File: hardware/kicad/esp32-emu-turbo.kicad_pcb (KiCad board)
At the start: 4 copper layers, 160 x 75 mm, 81 parts, among them J1 USB-C-16P, J3 JST-PH-2P, J4 FPC-40P-0.5mm, SW1 SW-SMD-5.1x5.1, SW10 SW-SMD-5.1x5.1, SW11 SW-SMD-5.1x5.1, SW12 SW-SMD-5.1x5.1, SW13 SW-SMD-5.1x5.1, SW2 SW-SMD-5.1x5.1, SW3 SW-SMD-5.1x5.1, SW4 SW-SMD-5.1x5.1, SW5 SW-SMD-5.1x5.1, SW6 SW-SMD-5.1x5.1, SW7 SW-SMD-5.1x5.1, SW8 SW-SMD-5.1x5.1, SW9 SW-SMD-5.1x5.1, U1 ESP32-S3-WROOM-1-N16R8, U2 ESOP-8, U3 SOT-223, U5 SOP-16, U6 TF-01A

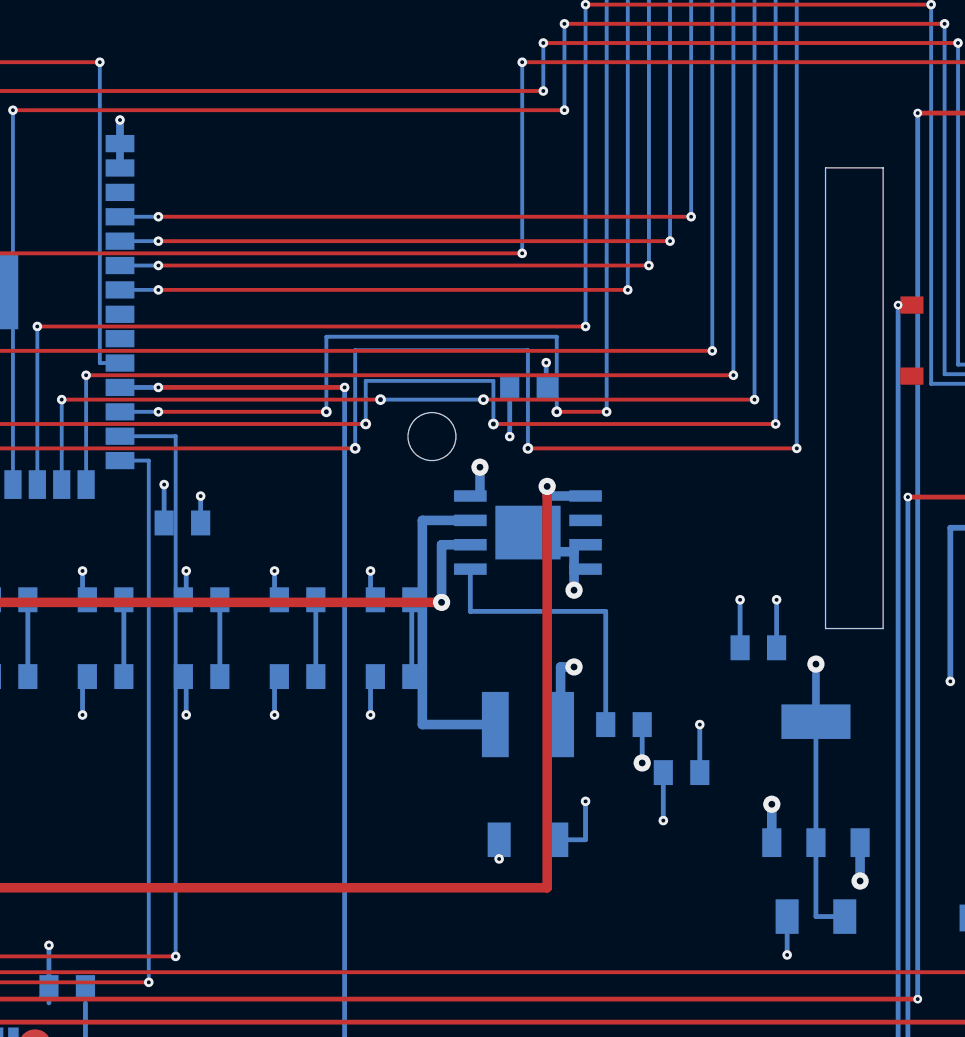
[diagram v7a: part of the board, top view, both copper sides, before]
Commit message: fix(pcb): thermal vias AMS1117 + LED nets + power trace widening
P1: Add 4 thermal vias (0.50/0.20mm) under AMS1117 tab pad for
    heat dissipation to In2.Cu +3V3 zone (0.85W at load)
P3: Add LED1_RA/LED2_RA nets for R17→LED1 and R18→LED2 connections
    (charging indicator LEDs were unrouted)
P4: Widen +3V3 main delivery traces from 0.4mm to 0.5mm (W_PWR)

Known remaining: BTN_X/Y F.Cu channels cross J1 shield pads
(structural issue requiring architectural reroute)

Results: 114/114 DFM + 9/9 DFA

Co-Authored-By: Claude Opus 4.6 (1M context) <noreply@anthropic.com>
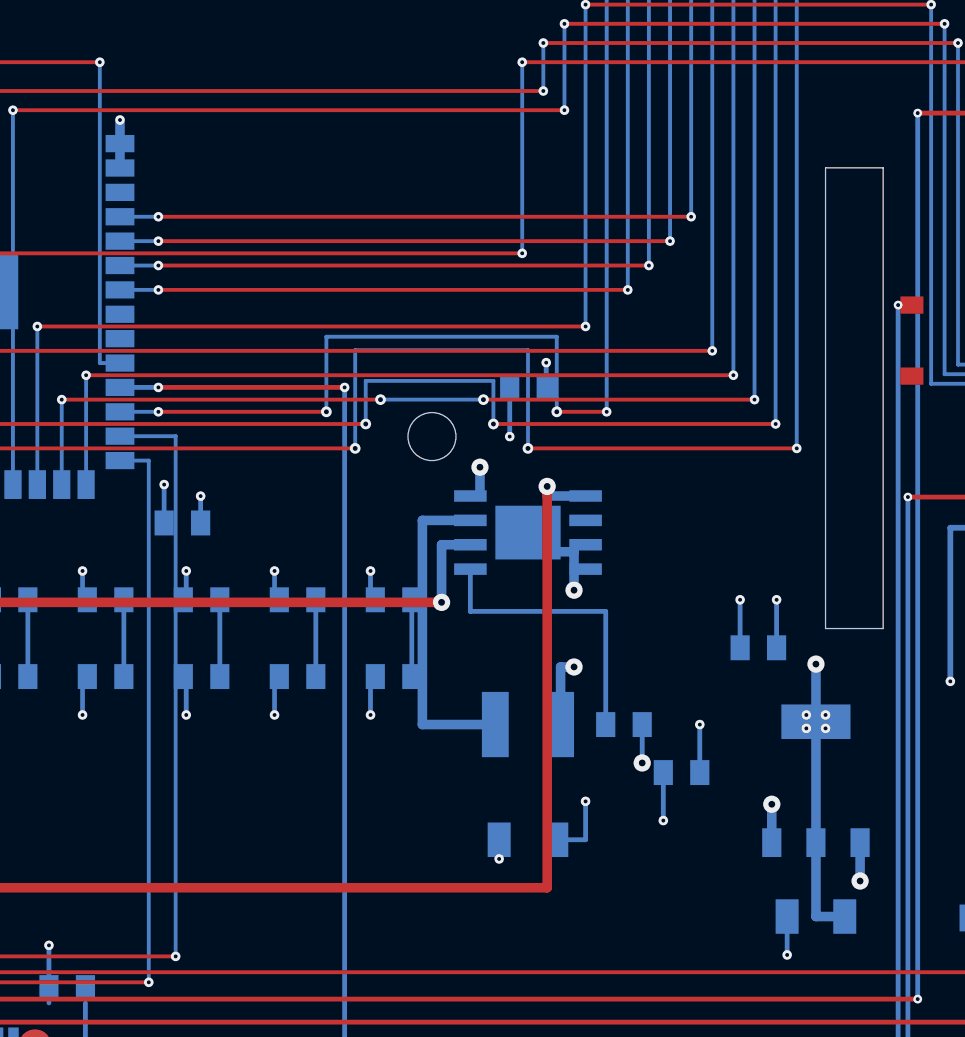
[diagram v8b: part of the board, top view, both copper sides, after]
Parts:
- removed the C25 at (31.5, 37.5)
- removed the SW10 at (28.0, 54.5)
- added FID1: Fiducial, Fiducial, F.Cu at (5.00, 5.00)
- added LED1: LED_0805, LED_0805, F.Cu at (25.0, 67.5)
- C25: renamed from FID1; value Fiducial -> C_0805; footprint Fiducial -> C_0805; moved to B.Cu
- SW10: renamed from LED1; value LED_0805 -> SW-SMD-5.1x5.1; footprint LED_0805 -> SW-SMD-5.1x5.1
- moved C25 41.9 mm to (31.5, 37.5)
- moved SW10 13.3 mm to (28.0, 54.5)
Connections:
- C25 pad 1: (no net) -> +5V
- LED2 pad 2: (no net) -> LED2_RA
- R17 pad 1: (no net) -> LED1_RA
- R18 pad 1: (no net) -> LED2_RA
- SW10 pad 1: GND -> (no net)
- SW10 pad 2: (no net) -> BTN_SELECT
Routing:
- net (no net): track 5.00 -> 0.00 mm, vias 2 -> 0
- net LED2_RA: track 0.00 -> 2.50 mm, vias 0 -> 1
- net LED1_RA: track 0.00 -> 2.50 mm, vias 0 -> 1
- net +3V3: track 59.1 -> 61.1 mm, vias 22 -> 26
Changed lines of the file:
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@@
   (net 49 "USB_CC2")
   (net 50 "PAM_VREF")
+  (net 51 "LED1_RA")
+  (net 52 "LED2_RA")
   (gr_line (start 6.0 0) (end 154.0 0) (stroke (width 0.05) (type default)) (layer "Edge.Cuts"))
   (gr_line (start 160.0 6.0) (end 160.0 69.0) (stroke (width 0.05) (type default)) (layer "Edge.Cuts"))
@@
     (property "Value" "LED_0805" (at 0 3 0) (layer "F.Fab") (effects (font (size 0.6 0.6) (thickness 0.2))))
     (pad "1" smd rect (at -0.95 0) (size 1.0 1.3) (layers "F.Cu" "F.Paste" "F.Mask") (net 1 "GND"))
-    (pad "2" smd rect (at 0.95 0) (size 1.0 1.3) (layers "F.Cu" "F.Paste" "F.Mask") (net 0 ""))
+    (pad "2" smd rect (at 0.95 0) (size 1.0 1.3) (layers "F.Cu" "F.Paste" "F.Mask") (net 51 "LED1_RA"))
   )
   (footprint "LED_0805" (at 32.0 67.5) (layer "F.Cu")
@@
     (property "Value" "LED_0805" (at 0 3 0) (layer "F.Fab") (effects (font (size 0.6 0.6) (thickness 0.2))))
     (pad "1" smd rect (at -0.95 0) (size 1.0 1.3) (layers "F.Cu" "F.Paste" "F.Mask") (net 1 "GND"))
-    (pad "2" smd rect (at 0.95 0) (size 1.0 1.3) (layers "F.Cu" "F.Paste" "F.Mask") (net 0 ""))
+    (pad "2" smd rect (at 0.95 0) (size 1.0 1.3) (layers "F.Cu" "F.Paste" "F.Mask") (net 52 "LED2_RA"))
   )
   (footprint "ESP32-S3-WROOM-1-N16R8" (at 80.0 27.5) (layer "B.Cu")
@@
     (property "Reference" "R17" (at 0 -3 0) (layer "B.Fab") (effects (font (size 0.6 0.6) (thickness 0.2)) (justify mirror)))
     (property "Value" "R_0805" (at 0 3 0) (layer "B.Fab") (effects (font (size 0.6 0.6) (thickness 0.2)) (justify mirror)))
-    (pad "1" smd rect (at 0.95 0) (size 1.0 1.3) (layers "B.Cu" "B.Paste" "B.Mask") (net 0 ""))
+    (pad "1" smd rect (at 0.95 0) (size 1.0 1.3) (layers "B.Cu" "B.Paste" "B.Mask") (net 51 "LED1_RA"))
     (pad "2" smd rect (at -0.95 0) (size 1.0 1.3) (layers "B.Cu" "B.Paste" "B.Mask") (net 4 "+3V3"))
   )
@@
     (property "Reference" "R18" (at 0 -3 0) (layer "B.Fab") (effects (font (size 0.6 0.6) (thickness 0.2)) (justify mirror)))
     (property "Value" "R_0805" (at 0 3 0) (layer "B.Fab") (effects (font (size 0.6 0.6) (thickness 0.2)) (justify mirror)))
-    (pad "1" smd rect (at 0.95 0) (size 1.0 1.3) (layers "B.Cu" "B.Paste" "B.Mask") (net 0 ""))
+    (pad "1" smd rect (at 0.95 0) (size 1.0 1.3) (layers "B.Cu" "B.Paste" "B.Mask") (net 52 "LED2_RA"))
     (pad "2" smd rect (at -0.95 0) (size 1.0 1.3) (layers "B.Cu" "B.Paste" "B.Mask") (net 4 "+3V3"))
   )
@@
   (segment (start 115.95 52.5) (end 115.95 54.5) (width 0.25) (layer "B.Cu") (net 3))
   (via (at 115.95 54.5) (size 0.9) (drill 0.35) (layers "F.Cu" "B.Cu") (net 3))
-  (segment (start 125.0 52.35) (end 125.0 49.35) (width 0.4) (layer "B.Cu") (net 4))
+  (segment (start 125.0 52.35) (end 125.0 49.35) (width 0.5) (layer "B.Cu") (net 4))
   (via (at 125.0 49.35) (size 0.9) (drill 0.35) (layers "F.Cu" "B.Cu") (net 4))
+  (via (at 124.5 52.0) (size 0.5) (drill 0.2) (layers "F.Cu" "B.Cu") (net 4))
+  (segment (start 124.5 52.0) (end 125.0 52.0) (width 0.5) (layer "B.Cu") (net 4))
+  (via (at 125.5 52.0) (size 0.5) (drill 0.2) (layers "F.Cu" "B.Cu") (net 4))
+  (segment (start 125.5 52.0) (end 125.0 52.0) (width 0.5) (layer "B.Cu") (net 4))
+  (via (at 124.5 52.7) (size 0.5) (drill 0.2) (layers "F.Cu" "B.Cu") (net 4))
+  (segment (start 124.5 52.7) (end 125.0 52.7) (width 0.5) (layer "B.Cu") (net 4))
+  (via (at 125.5 52.7) (size 0.5) (drill 0.2) (layers "F.Cu" "B.Cu") (net 4))
+  (segment (start 125.5 52.7) (end 125.0 52.7) (width 0.5) (layer "B.Cu") (net 4))
   (via (at 88.75 21.01) (size 0.5) (drill 0.2) (layers "F.Cu" "B.Cu") (net 4))
-  (segment (start 88.75 23.51) (end 88.75 21.01) (width 0.4) (layer "B.Cu") (net 4))
+  (segment (start 88.75 23.51) (end 88.75 21.01) (width 0.5) (layer "B.Cu") (net 4))
   (segment (start 107.0 43.135) (end 105.5 43.135) (width 0.5) (layer "B.Cu") (net 5))
   (segment (start 105.5 43.135) (end 105.5 46.135) (width 0.5) (layer "B.Cu") (net 5))
@@
   (segment (start 121.05 48.5) (end 121.05 46.0) (width 0.25) (layer "B.Cu") (net 1))
   (via (at 121.05 46.0) (size 0.5) (drill 0.2) (layers "F.Cu" "B.Cu") (net 1))
-  (segment (start 126.5 62.5) (end 125.0 62.5) (width 0.25) (layer "B.Cu") (net 4))
-  (segment (start 125.0 62.5) (end 125.0 52.35) (width 0.25) (layer "B.Cu") (net 4))
+  (segment (start 126.5 62.5) (end 125.0 62.5) (width 0.5) (layer "B.Cu") (net 4))
+  (segment (start 125.0 62.5) (end 125.0 52.35) (width 0.5) (layer "B.Cu") (net 4))
   (segment (start 123.5 62.5) (end 123.5 64.5) (width 0.25) (layer "B.Cu") (net 1))
   (via (at 123.5 64.5) (size 0.5) (drill 0.2) (layers "F.Cu" "B.Cu") (net 1))
@@
   (via (at 24.05 62.65) (size 0.5) (drill 0.2) (layers "F.Cu" "B.Cu") (net 4))
   (segment (start 24.05 62.65) (end 24.05 65.0) (width 0.25) (layer "B.Cu") (net 4))
-  (segment (start 25.95 65.0) (end 25.95 66.25) (width 0.25) (layer "B.Cu") (net 0))
-  (via (at 25.95 66.25) (size 0.8) (drill 0.35) (layers "F.Cu" "B.Cu") (net 0))
-  (segment (start 25.95 66.25) (end 25.95 67.5) (width 0.25) (layer "F.Cu") (net 0))
+  (segment (start 25.95 65.0) (end 25.95 66.25) (width 0.25) (layer "B.Cu") (net 51))
+  (via (at 25.95 66.25) (size 0.8) (drill 0.35) (layers "F.Cu" "B.Cu") (net 51))
+  (segment (start 25.95 66.25) (end 25.95 67.5) (width 0.25) (layer "F.Cu") (net 51))
   (segment (start 24.05 67.5) (end 23.35 67.5) (width 0.25) (layer "F.Cu") (net 1))
   (via (at 23.35 67.5) (size 0.5) (drill 0.2) (layers "F.Cu" "B.Cu") (net 1))
   (via (at 31.05 62.65) (size 0.5) (drill 0.2) (layers "F.Cu" "B.Cu") (net 4))
   (segment (start 31.05 62.65) (end 31.05 65.0) (width 0.25) (layer "B.Cu") (net 4))
-  (segment (start 32.95 65.0) (end 32.95 66.25) (width 0.25) (layer "B.Cu") (net 0))
-  (via (at 32.95 66.25) (size 0.8) (drill 0.35) (layers "F.Cu" "B.Cu") (net 0))
-  (segment (start 32.95 66.25) (end 32.95 67.5) (width 0.25) (layer "F.Cu") (net 0))
+  (segment (start 32.95 65.0) (end 32.95 66.25) (width 0.25) (layer "B.Cu") (net 52))
+  (via (at 32.95 66.25) (size 0.8) (drill 0.35) (layers "F.Cu" "B.Cu") (net 52))
+  (segment (start 32.95 66.25) (end 32.95 67.5) (width 0.25) (layer "F.Cu") (net 52))
   (segment (start 31.05 67.5) (end 30.35 67.5) (width 0.25) (layer "F.Cu") (net 1))
   (via (at 30.35 67.5) (size 0.5) (drill 0.2) (layers "F.Cu" "B.Cu") (net 1))
